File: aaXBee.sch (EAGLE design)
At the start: 82 parts, among them Q1 IRLML6244TR, SW1 RESET, SW7 SW7, U1 ATmega328P-AU, U2 DS3231, U3 MCP9808, U4 MCP1640D, U5 MCP1640D, Y1 8MHz

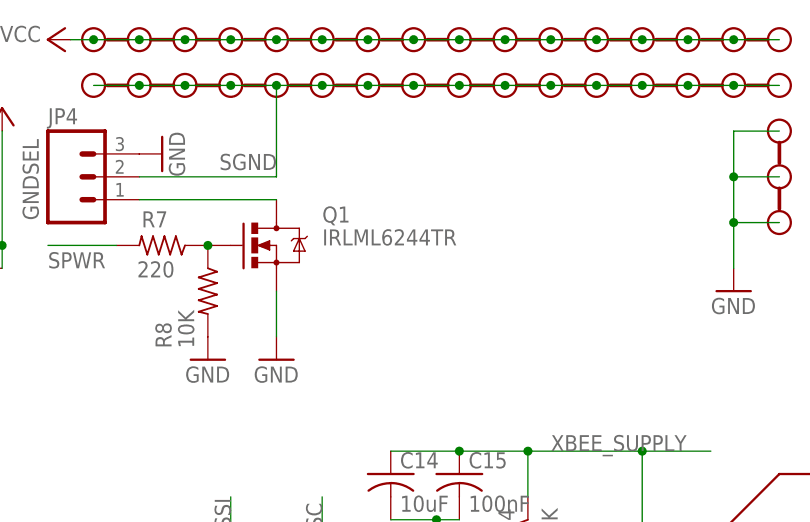
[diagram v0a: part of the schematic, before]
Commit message: Improved footprint for U3, change Q1 to Si2302CDS, added documentation and photos.
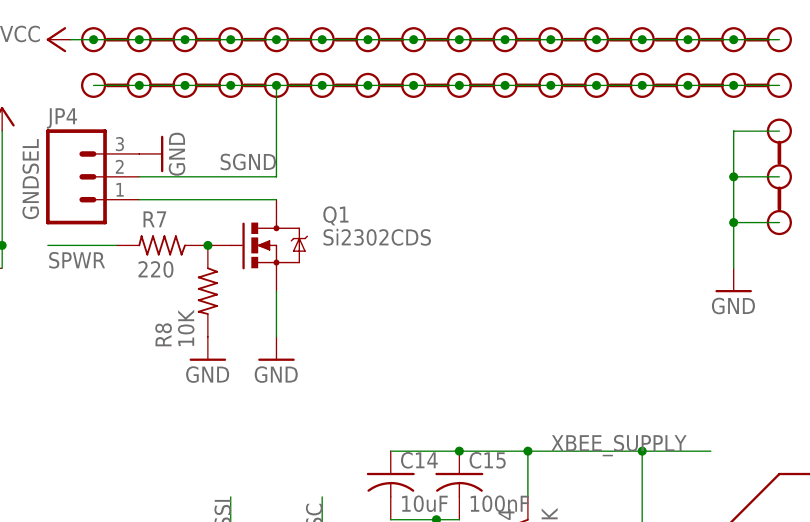
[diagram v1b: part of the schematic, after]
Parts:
- Q1: value IRLML6244TR -> Si2302CDS
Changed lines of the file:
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@@
 <part name="PR12" library="_jc" deviceset="PROTO-10" device=""/>
 <part name="P+6" library="supply1" deviceset="VCC" device=""/>
-<part name="Q1" library="_jc" deviceset="MOSFET-NCHANNEL" device="SOT23" value="IRLML6244TR"/>
+<part name="Q1" library="_jc" deviceset="MOSFET-NCHANNEL" device="SOT23" value="Si2302CDS"/>
 <part name="GND25" library="supply1" deviceset="GND" device=""/>
 <part name="R7" library="_jc" deviceset="R-US_" device="M0805" value="220"/>

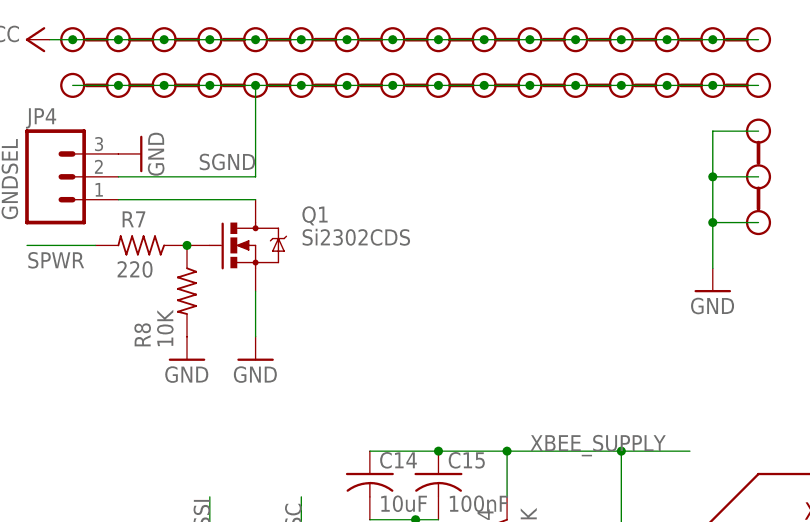
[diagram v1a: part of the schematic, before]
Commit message: Change Q1 to IRLML6344TRPBF.
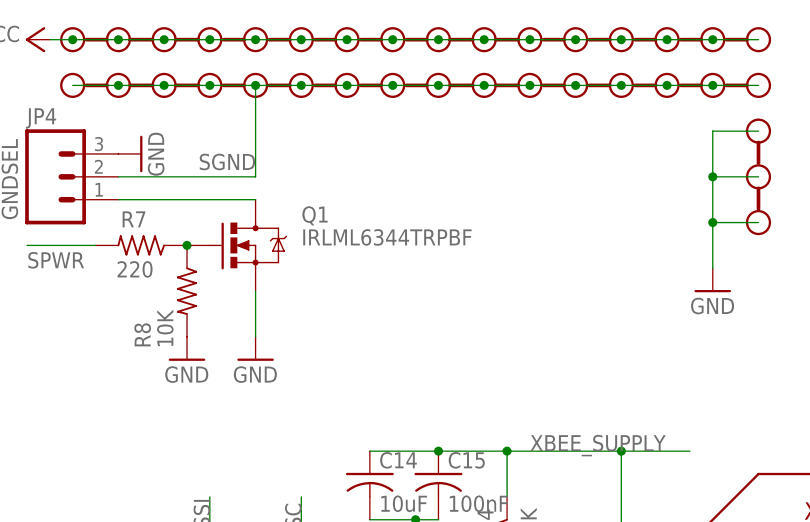
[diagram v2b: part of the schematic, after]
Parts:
- Q1: value Si2302CDS -> IRLML6344TRPBF
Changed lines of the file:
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@@
 <part name="PR12" library="_jc" deviceset="PROTO-10" device=""/>
 <part name="P+6" library="supply1" deviceset="VCC" device=""/>
-<part name="Q1" library="_jc" deviceset="MOSFET-NCHANNEL" device="SOT23" value="Si2302CDS"/>
+<part name="Q1" library="_jc" deviceset="MOSFET-NCHANNEL" device="SOT23" value="IRLML6344TRPBF"/>
 <part name="GND25" library="supply1" deviceset="GND" device=""/>
 <part name="R7" library="_jc" deviceset="R-US_" device="M0805" value="220"/>
